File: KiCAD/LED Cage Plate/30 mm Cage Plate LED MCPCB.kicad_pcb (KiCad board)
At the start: 2 copper layers, 40 x 40 mm, 27 parts, among them IC1 AL8843QSP-13, J1 Conn_01x08_Socket, J2 0, Q5 2x_p-channel, Q6 2x_p-channel

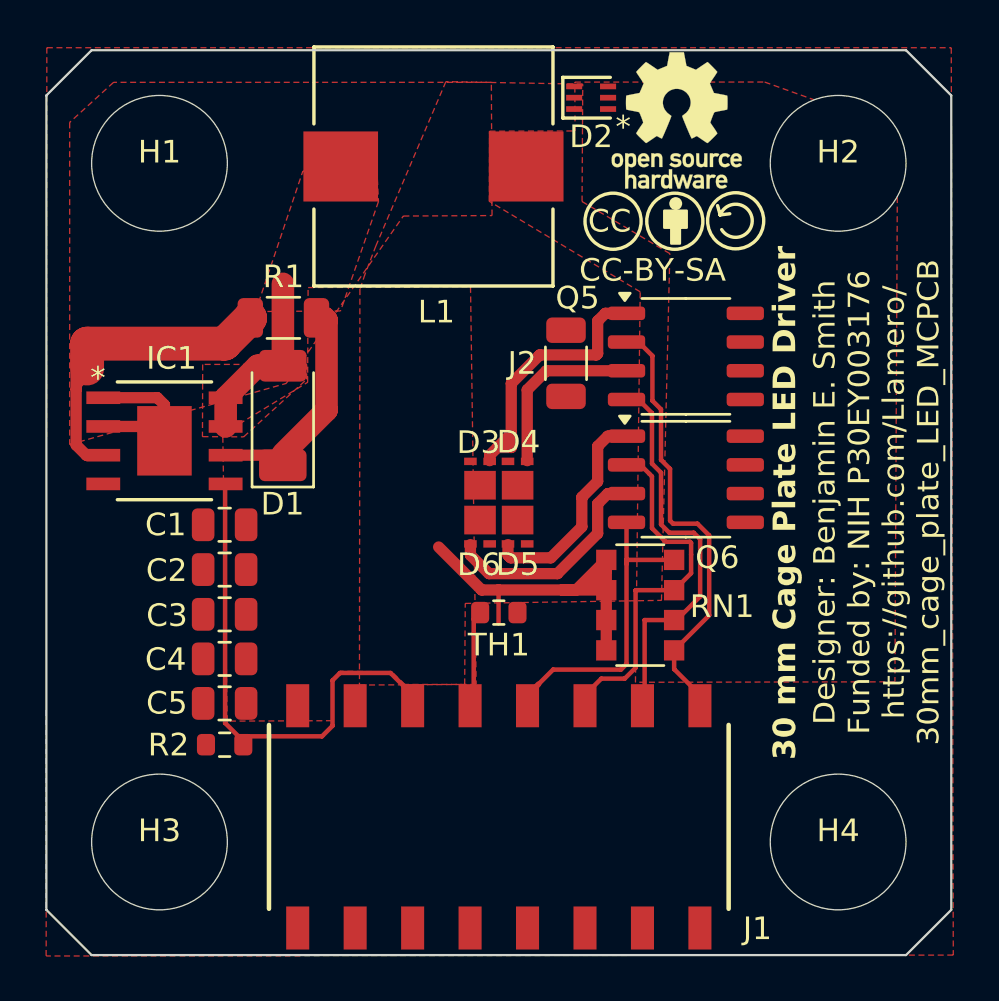
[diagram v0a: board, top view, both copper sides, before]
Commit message: Improve clearance of gate traces on LED plate
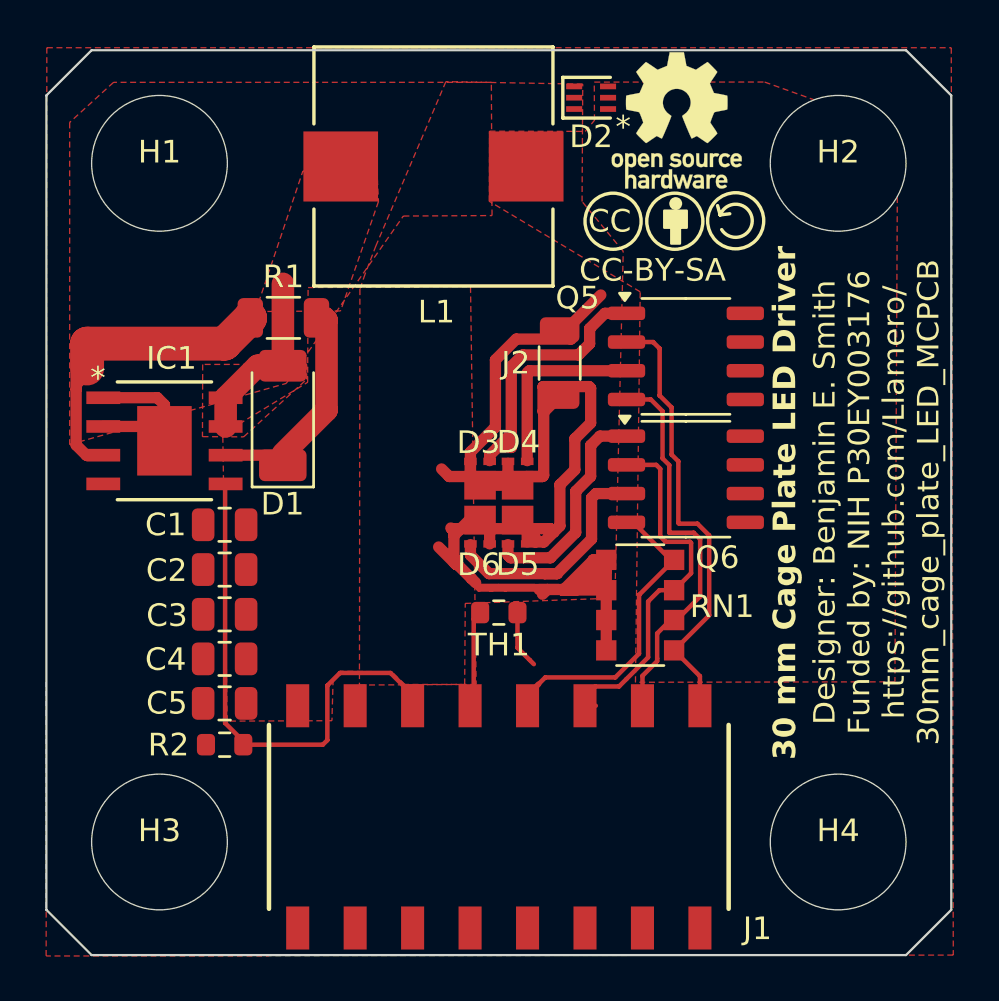
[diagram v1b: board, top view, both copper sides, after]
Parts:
- L1: value 15μH -> 47μH
- moved J2 0.28 mm to (122.7, 73.8)
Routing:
- net /LED+: track 32.7 -> 90.2 mm
- net GND: track 7.39 -> 9.97 mm
- net Net-(D6-K): track 9.94 -> 10.8 mm
- net /3: track 16.9 -> 17.6 mm
- net /PWM: track 22.9 -> 23.6 mm

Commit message: update
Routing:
- net /LED+: track 90.2 -> 87.3 mm
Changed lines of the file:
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@@
-	)
-	(segment
-		(start 119.1192 83.8392)
-		(end 119.65 83.8392)
-		(width 0.2)
-		(layer "F.Cu")
-		(net 7)
 	)
 	(segment
@@
 	)
 	(segment
-		(start 119.65 83.8392)
-		(end 119.6888 83.8392)
-		(width 0.2)
-		(layer "F.Cu")
-		(net 7)
-	)
-	(segment
 		(start 119.12565 83.6892)
 		(end 120 83.6892)
@@
 	)
 	(segment
-		(start 118.978225 83.698225)
-		(end 119.1192 83.8392)
-		(width 0.2)
-		(layer "F.Cu")
-		(net 7)
-	)
-	(segment
 		(start 124.06 76.48005)
 		(end 123.36 77.18005)
@@
 	)
 	(segment
-		(start 120.29 83.8392)
-		(end 121.78 83.8392)
-		(width 0.2)
-		(layer "F.Cu")
-		(net 7)
-	)
-	(segment
 		(start 119.12565 83.6892)
 		(end 122.6292 83.6892)
@@
 		(layer "F.Cu")
 		(net 7)
-	)
-	(segment
-		(start 119.65 83.8392)
-		(end 120.29 83.8392)
-		(width 0.2)
-		(layer "F.Cu")
-		(net 7)

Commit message: Working draft of series LED - passes DRC
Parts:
- removed D2: D_Zener, Custom:DFN6_TDS3011_SEM
- removed J2: 0, Resistor_SMD:R_1206_3216Metric
- removed Q5, Q6: 2x_p-channel, Custom:SOP-8_3.9x4.9mm_P1.27mm
- removed RN1: 4700, Resistor_SMD:R_Array_Convex_4x1206
- added D11: D_Zener, Custom:DFN6_TDS3011_SEM, F.Cu at (129.3, 62.0)
- added Q1: Q_PMOS, Custom:SON8_DMP4025SFGQ-13_DIO, F.Cu at (113.6, 63.4)
- added Q2: Q_NMOS, Package_TO_SOT_SMD:SOT-23, F.Cu at (127.6, 85.6)
- added R3: 10k, Resistor_SMD:R_0603_1608Metric, F.Cu at (124.4, 86.8)
- R2: value 4700 -> 10k
- moved R2 27.3 mm to (110.6, 63.5), turned to -90 degrees
- moved SYM2 11.4 mm to (127.4, 78.7)
- moved SYM1 11.4 mm to (127.3, 74.5)
- moved L1 5.06 mm to (122.2, 65.4)
- moved IC1 0.64 mm to (105.9, 77.2)
- moved D1 0.64 mm to (111.1, 76.1)
- moved R1 0.64 mm to (111.1, 71.8)
- turned TH1 to 0 degrees
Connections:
- D3 pad 2: /LED+ -> Net-(D3-A)
- D3 pad 3: /LED+ -> Net-(D3-A)
- D4 pad 2: /LED+ -> Net-(D3-K)
- D4 pad 3: /LED+ -> Net-(D3-A)
- D5 pad 2: /LED+ -> Net-(D4-K)
- D5 pad 3: /LED+ -> Net-(D3-A)
- D6 pad 1: Net-(D6-K) -> /LED-
- D6 pad 2: /LED+ -> Net-(D5-K)
- D6 pad 3: /LED+ -> Net-(D3-A)
- J1 pad 4: /Temp -> GND
- J1 pad 5: /4 -> /Temp
- J1 pad 6: /3 -> GND
- J1 pad 7: /2 -> /Gate
- J1 pad 8: /1 -> GND
- R2 pad 1: /PWM -> /LED+
- R2 pad 2: GND -> Net-(Q1-G)
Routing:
- net Net-(Q1-G): track 0.00 -> 54.4 mm
- net /LED+: track 87.3 -> 33.3 mm
- net /1: track 20.6 -> 0.00 mm
- net /2: track 18.1 -> 0.00 mm
- net /3: track 17.6 -> 0.00 mm
- net /4: track 14.0 -> 0.00 mm
- net Net-(D3-K): track 12.2 -> 0.81 mm
- net Net-(D6-K): track 10.8 -> 0.00 mm
- net Net-(D5-K): track 9.85 -> 0.81 mm
- net GND: track 9.97 -> 14.3 mm
- net /Gate: track 0.00 -> 4.19 mm
- net Net-(D4-K): track 8.31 -> 4.97 mm
- net /LED-: track 0.00 -> 0.88 mm
- net /PWM: track 23.6 -> 23.0 mm
- added copper zone on F.Cu, net Net-(D3-A)
